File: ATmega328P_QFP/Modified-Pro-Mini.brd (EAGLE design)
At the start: 18.3 x 33.5 mm, 17 parts, among them Q1 8/16/20MHz, U1 ATMEGA328

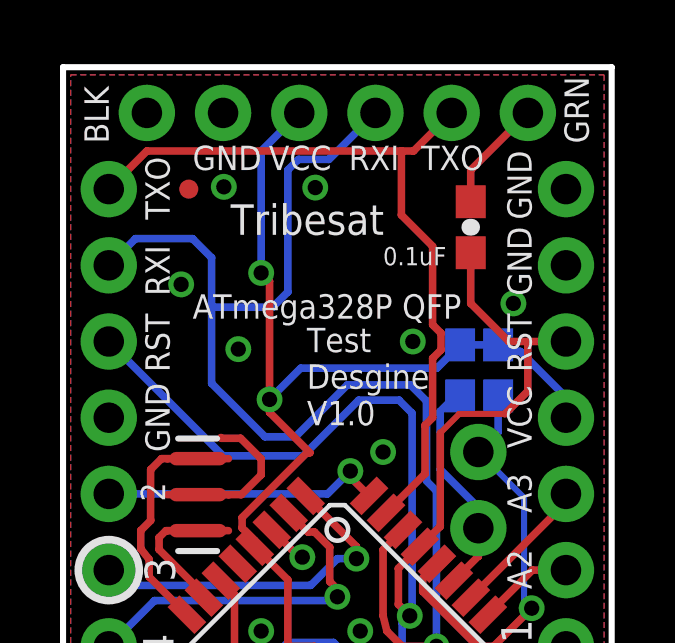
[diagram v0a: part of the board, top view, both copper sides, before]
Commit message: added decoupling cap
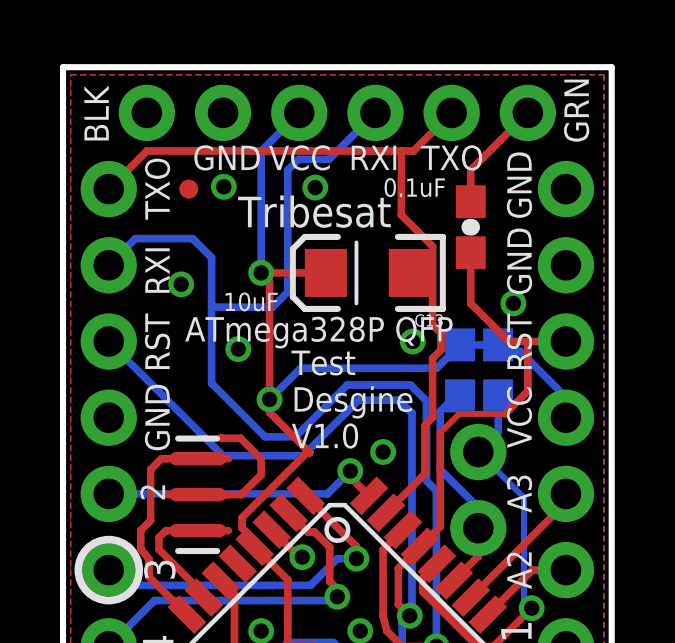
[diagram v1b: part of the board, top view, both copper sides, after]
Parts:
- added C13: 10uF, SparkFun:EIA3216
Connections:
- net GND: now also C13.C
- net VCC: now also C13.A
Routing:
- net VCC: track 54.4 -> 56.6 mm
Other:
- board text added: "10uF"
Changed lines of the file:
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@@
 <rectangle x1="5.334" y1="0.635" x2="5.969" y2="1.27" layer="22"/>
 <text x="15.367" y="28.194" size="0.8128" layer="21" ratio="15" rot="R90">GND</text>
-<text x="5.334" y="27.686" size="1.016" layer="21" font="vector" ratio="15">Tribesat</text>
-<text x="4.064" y="24.892" size="0.8128" layer="21" font="vector" ratio="15">ATmega328P QFP</text>
-<text x="7.874" y="21.336" size="0.8128" layer="21" font="vector" ratio="15">Test
+<text x="5.588" y="27.94" size="1.016" layer="21" font="vector" ratio="15">Tribesat</text>
+<text x="3.81" y="24.13" size="0.8128" layer="21" font="vector" ratio="15">ATmega328P QFP</text>
+<text x="7.366" y="20.574" size="0.8128" layer="21" font="vector" ratio="15">Test
 Desgine
 V1.0</text>
@@
 <text x="5.334" y="1.524" size="0.6096" layer="21" font="vector" ratio="13">0.1uF</text>
 <text x="6.604" y="3.81" size="0.6096" layer="21" font="vector" ratio="13">10k</text>
-<text x="10.414" y="26.67" size="0.6096" layer="21" font="vector" ratio="13">0.1uF</text>
+<text x="10.414" y="28.956" size="0.6096" layer="21" font="vector" ratio="13">0.1uF</text>
 <text x="5.334" y="28.702" size="1.016" layer="22" font="vector" ratio="16" rot="MR180">Tribesat</text>
 <text x="14.224" y="24.892" size="0.8128" layer="22" font="vector" ratio="16" rot="MR0">ATmega328P QFP</text>
@@
 Desgine
 V1.0</text>
+<text x="5.08" y="25.146" size="0.6096" layer="21" font="vector" ratio="13">10uF</text>
 </plain>
 <attributes>
@@
 <attribute name="VALUE" x="14.478" y="26.924" size="0.4064" layer="27" font="vector" rot="R90"/>
 </element>
+<element name="C13" library="SparkFun" package="EIA3216" value="10uF" x="9.906" y="26.416" rot="R180"/>
 </elements>
 <signals>
@@
 <via x="12.7" y="5.588" extent="1-16" drill="0.508"/>
 <contactref element="JP6" pad="1"/>
+<contactref element="C13" pad="C"/>
 </signal>
 <signal name="AREF">
@@
 <wire x1="6.6294" y1="22.1996" x2="6.6294" y2="26.1366" width="0.254" layer="1"/>
 <wire x1="6.6294" y1="26.1366" x2="6.35" y2="26.416" width="0.254" layer="1"/>
+<contactref element="C13" pad="A"/>
+<wire x1="6.35" y1="26.416" x2="8.506" y2="26.416" width="0.254" layer="1"/>
 </signal>
 <signal name="D9">

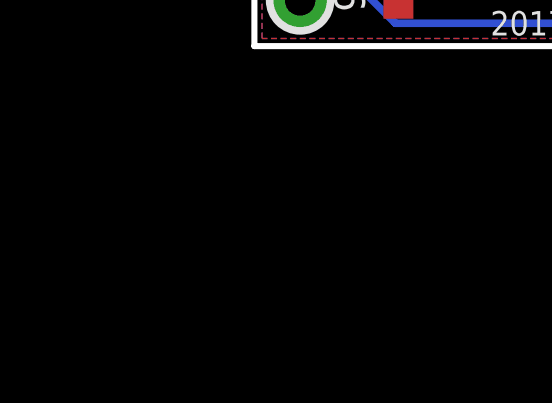
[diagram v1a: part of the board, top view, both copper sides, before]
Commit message: added decoupling cap
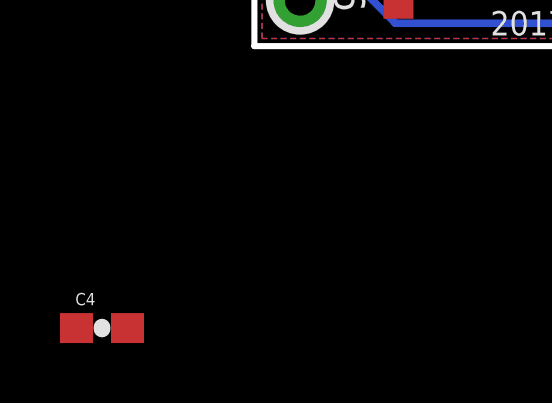
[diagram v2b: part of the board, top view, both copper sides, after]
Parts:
- added C4: 0.1uF, SparkFun:0603-CAP
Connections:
- net GND: now also C4.1
- net VCC: now also C4.2
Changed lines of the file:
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@@
 </element>
 <element name="C13" library="SparkFun" package="EIA3216" value="10uF" x="9.906" y="26.416" rot="R180"/>
+<element name="C4" library="SparkFun" package="0603-CAP" value="0.1uF" x="-5.334" y="-9.652"/>
 </elements>
 <signals>
@@
 <contactref element="JP6" pad="1"/>
 <contactref element="C13" pad="C"/>
+<contactref element="C4" pad="1"/>
+<wire x1="16.51" y1="26.67" x2="16.51" y2="29.21" width="0" layer="19" extent="1-1"/>
+<wire x1="14.7574" y1="25.4" x2="16.51" y2="26.67" width="0" layer="19" extent="1-1"/>
+<wire x1="11.306" y1="26.416" x2="14.7574" y2="25.4" width="0" layer="19" extent="1-1"/>
+<wire x1="11.4046" y1="24.13" x2="11.306" y2="26.416" width="0" layer="19" extent="1-1"/>
+<wire x1="10.414" y1="20.447" x2="11.4046" y2="24.13" width="0" layer="19" extent="1-1"/>
+<wire x1="6.35" y1="20.2184" x2="10.414" y2="20.447" width="0" layer="19" extent="1-1"/>
+<wire x1="6.7032" y1="17.853853125" x2="5.6896" y2="19.0246" width="0" layer="19" extent="1-1"/>
+<wire x1="7.7216" y1="16.9418" x2="7.666053125" y2="16.891" width="0" layer="19" extent="1-1"/>
+<wire x1="5.571828125" y1="16.72248125" x2="6.7032" y2="17.853853125" width="0" layer="19" extent="1-1"/>
+<wire x1="6.35" y1="14.478" x2="5.571828125" y2="16.72248125" width="0" layer="19" extent="1-1"/>
+<wire x1="5.588" y1="23.876" x2="5.6642" y2="20.9042" width="0" layer="19" extent="1-1"/>
+<wire x1="3.683" y1="26.035" x2="5.588" y2="23.876" width="0" layer="19" extent="1-1"/>
+<wire x1="9.652" y1="14.478" x2="7.747" y2="16.891" width="0" layer="19" extent="1-1"/>
+<wire x1="11.43" y1="12.7" x2="9.652" y2="14.478" width="0" layer="19" extent="1-1"/>
+<wire x1="12.20816875" y1="11.217515625" x2="11.43" y2="12.7" width="0" layer="19" extent="1-1"/>
+<wire x1="1.27" y1="21.59" x2="3.2258" y2="19.0246" width="0" layer="19" extent="1-1"/>
+<wire x1="5.1054" y1="29.2862" x2="3.683" y2="26.035" width="0" layer="19" extent="1-1"/>
+<wire x1="5.08" y1="31.75" x2="5.1054" y2="29.2862" width="0" layer="19" extent="1-1"/>
+<wire x1="2.54" y1="31.75" x2="5.08" y2="31.75" width="0" layer="19" extent="1-1"/>
+<wire x1="8.1534" y1="29.2608" x2="5.1054" y2="29.2862" width="0" layer="19" extent="1-1"/>
+<wire x1="9.867" y1="7.239" x2="12.20816875" y2="11.217515625" width="0" layer="19" extent="1-1"/>
+<wire x1="12.7" y1="5.588" x2="9.867" y2="7.239" width="0" layer="19" extent="1-1"/>
+<wire x1="12.0262" y1="1.524" x2="12.7" y2="5.588" width="0" layer="19" extent="1-1"/>
+<wire x1="8.89" y1="2.667" x2="12.0262" y2="1.524" width="0" layer="19" extent="1-1"/>
+<wire x1="5.969" y1="1.651" x2="8.89" y2="2.667" width="0" layer="19" extent="1-1"/>
+<wire x1="-6.184" y1="-9.652" x2="4.5466" y2="1.2074" width="0" layer="19" extent="1-1"/>
 </signal>
 <signal name="AREF">
@@
 <contactref element="C13" pad="A"/>
 <wire x1="6.35" y1="26.416" x2="8.506" y2="26.416" width="0.254" layer="1"/>
+<contactref element="C4" pad="2"/>
+<wire x1="4.865" y1="5.08" x2="-4.484" y2="-9.652" width="0" layer="19" extent="1-1"/>
 </signal>
 <signal name="D9">

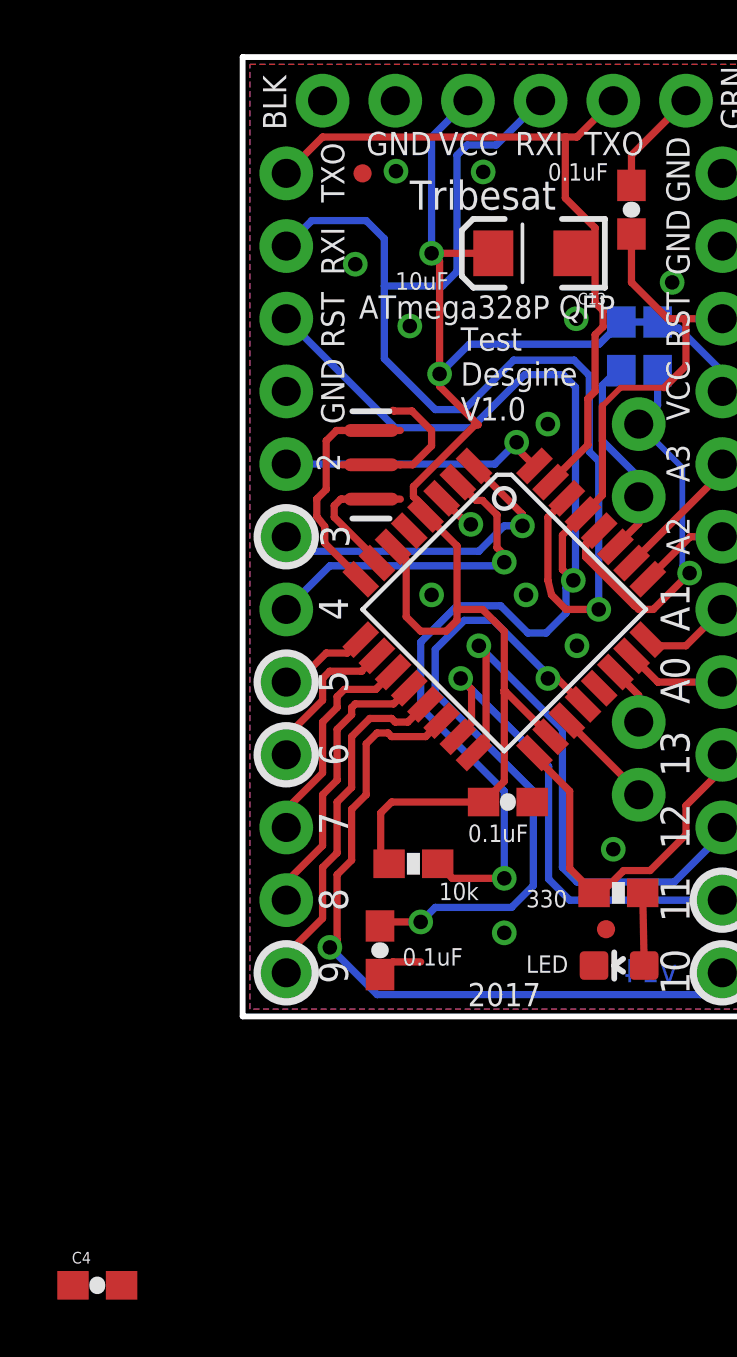
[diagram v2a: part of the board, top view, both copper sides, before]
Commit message: palced decoupling cap
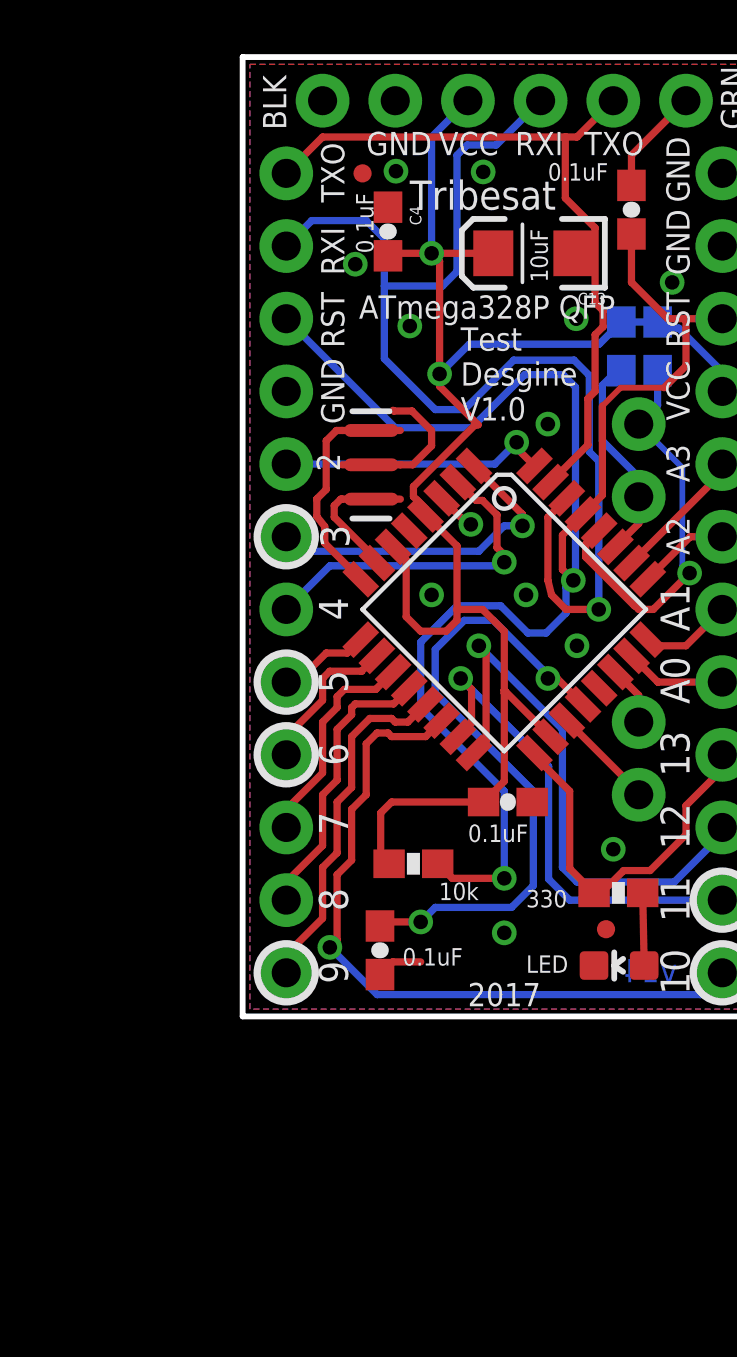
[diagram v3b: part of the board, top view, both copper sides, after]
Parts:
- moved C4 38.2 mm to (4.83, 27.2), turned to 270 degrees
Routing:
- net VCC: track 56.6 -> 58.2 mm
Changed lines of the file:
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@@
 Desgine
 V1.0</text>
-<text x="5.08" y="25.146" size="0.6096" layer="21" font="vector" ratio="13">10uF</text>
+<text x="10.414" y="25.4" size="0.6096" layer="21" font="vector" ratio="13" rot="R90">10uF</text>
+<text x="4.318" y="26.416" size="0.6096" layer="21" font="vector" ratio="13" rot="R90">0.1uF</text>
 </plain>
 <attributes>
@@
 </element>
 <element name="C13" library="SparkFun" package="EIA3216" value="10uF" x="9.906" y="26.416" rot="R180"/>
-<element name="C4" library="SparkFun" package="0603-CAP" value="0.1uF" x="-5.334" y="-9.652"/>
+<element name="C4" library="SparkFun" package="0603-CAP" value="0.1uF" x="4.826" y="27.178" rot="R270"/>
 </elements>
 <signals>
@@
 <contactref element="C13" pad="C"/>
 <contactref element="C4" pad="1"/>
-<wire x1="16.51" y1="26.67" x2="16.51" y2="29.21" width="0" layer="19" extent="1-1"/>
-<wire x1="14.7574" y1="25.4" x2="16.51" y2="26.67" width="0" layer="19" extent="1-1"/>
-<wire x1="11.306" y1="26.416" x2="14.7574" y2="25.4" width="0" layer="19" extent="1-1"/>
-<wire x1="11.4046" y1="24.13" x2="11.306" y2="26.416" width="0" layer="19" extent="1-1"/>
-<wire x1="10.414" y1="20.447" x2="11.4046" y2="24.13" width="0" layer="19" extent="1-1"/>
-<wire x1="6.35" y1="20.2184" x2="10.414" y2="20.447" width="0" layer="19" extent="1-1"/>
-<wire x1="6.7032" y1="17.853853125" x2="5.6896" y2="19.0246" width="0" layer="19" extent="1-1"/>
-<wire x1="7.7216" y1="16.9418" x2="7.666053125" y2="16.891" width="0" layer="19" extent="1-1"/>
-<wire x1="5.571828125" y1="16.72248125" x2="6.7032" y2="17.853853125" width="0" layer="19" extent="1-1"/>
-<wire x1="6.35" y1="14.478" x2="5.571828125" y2="16.72248125" width="0" layer="19" extent="1-1"/>
-<wire x1="5.588" y1="23.876" x2="5.6642" y2="20.9042" width="0" layer="19" extent="1-1"/>
-<wire x1="3.683" y1="26.035" x2="5.588" y2="23.876" width="0" layer="19" extent="1-1"/>
-<wire x1="9.652" y1="14.478" x2="7.747" y2="16.891" width="0" layer="19" extent="1-1"/>
-<wire x1="11.43" y1="12.7" x2="9.652" y2="14.478" width="0" layer="19" extent="1-1"/>
-<wire x1="12.20816875" y1="11.217515625" x2="11.43" y2="12.7" width="0" layer="19" extent="1-1"/>
-<wire x1="1.27" y1="21.59" x2="3.2258" y2="19.0246" width="0" layer="19" extent="1-1"/>
-<wire x1="5.1054" y1="29.2862" x2="3.683" y2="26.035" width="0" layer="19" extent="1-1"/>
-<wire x1="5.08" y1="31.75" x2="5.1054" y2="29.2862" width="0" layer="19" extent="1-1"/>
-<wire x1="2.54" y1="31.75" x2="5.08" y2="31.75" width="0" layer="19" extent="1-1"/>
-<wire x1="8.1534" y1="29.2608" x2="5.1054" y2="29.2862" width="0" layer="19" extent="1-1"/>
-<wire x1="9.867" y1="7.239" x2="12.20816875" y2="11.217515625" width="0" layer="19" extent="1-1"/>
-<wire x1="12.7" y1="5.588" x2="9.867" y2="7.239" width="0" layer="19" extent="1-1"/>
-<wire x1="12.0262" y1="1.524" x2="12.7" y2="5.588" width="0" layer="19" extent="1-1"/>
-<wire x1="8.89" y1="2.667" x2="12.0262" y2="1.524" width="0" layer="19" extent="1-1"/>
-<wire x1="5.969" y1="1.651" x2="8.89" y2="2.667" width="0" layer="19" extent="1-1"/>
-<wire x1="-6.184" y1="-9.652" x2="4.5466" y2="1.2074" width="0" layer="19" extent="1-1"/>
 </signal>
 <signal name="AREF">
@@
 <wire x1="6.35" y1="26.416" x2="8.506" y2="26.416" width="0.254" layer="1"/>
 <contactref element="C4" pad="2"/>
-<wire x1="4.865" y1="5.08" x2="-4.484" y2="-9.652" width="0" layer="19" extent="1-1"/>
+<wire x1="6.35" y1="26.416" x2="4.914" y2="26.416" width="0.254" layer="1"/>
+<wire x1="4.914" y1="26.416" x2="4.826" y2="26.328" width="0.254" layer="1"/>
 </signal>
 <signal name="D9">

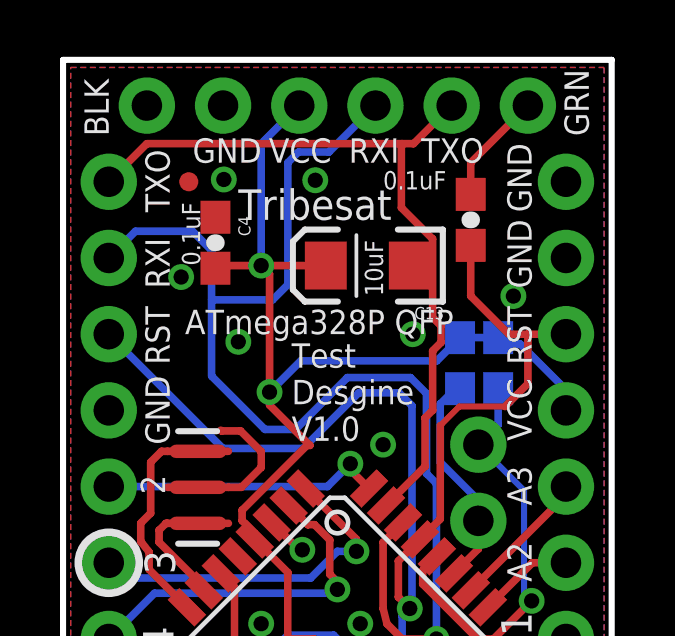
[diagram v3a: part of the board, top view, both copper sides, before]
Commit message: fixed DRC errors
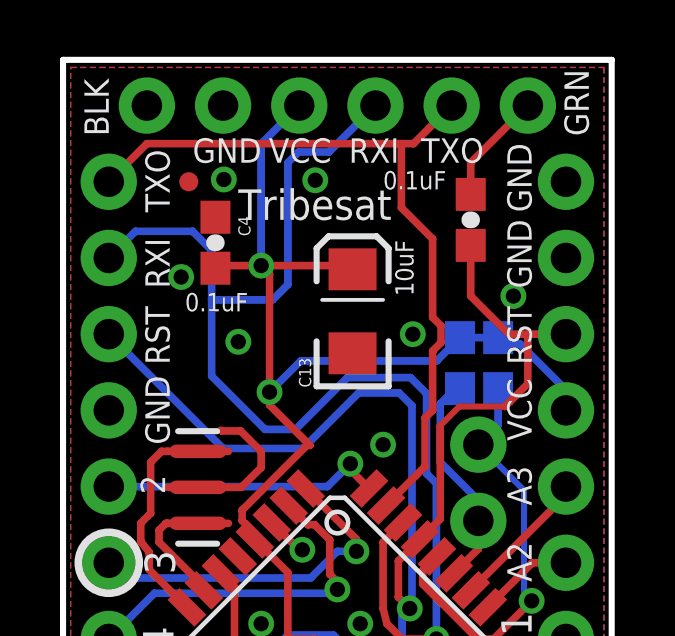
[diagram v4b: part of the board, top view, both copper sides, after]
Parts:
- moved C13 1.61 mm to (9.40, 24.9), turned to 90 degrees
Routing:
- net VCC: track 58.2 -> 59.1 mm
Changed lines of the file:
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@@
 <text x="15.367" y="28.194" size="0.8128" layer="21" ratio="15" rot="R90">GND</text>
 <text x="5.588" y="27.94" size="1.016" layer="21" font="vector" ratio="15">Tribesat</text>
-<text x="3.81" y="24.13" size="0.8128" layer="21" font="vector" ratio="15">ATmega328P QFP</text>
-<text x="7.366" y="20.574" size="0.8128" layer="21" font="vector" ratio="15">Test
-Desgine
-V1.0</text>
 <text x="8.89" y="0.508" size="0.8128" layer="21" font="vector" ratio="15" align="center">2017</text>
 <text x="7.62" y="5.842" size="0.6096" layer="21" font="vector" ratio="13">0.1uF</text>
@@
 Desgine
 V1.0</text>
-<text x="10.414" y="25.4" size="0.6096" layer="21" font="vector" ratio="13" rot="R90">10uF</text>
-<text x="4.318" y="26.416" size="0.6096" layer="21" font="vector" ratio="13" rot="R90">0.1uF</text>
+<text x="11.43" y="25.4" size="0.6096" layer="21" font="vector" ratio="13" rot="R90">10uF</text>
+<text x="3.81" y="24.892" size="0.6096" layer="21" font="vector" ratio="13">0.1uF</text>
 </plain>
 <attributes>
@@
 <attribute name="VALUE" x="14.478" y="26.924" size="0.4064" layer="27" font="vector" rot="R90"/>
 </element>
-<element name="C13" library="SparkFun" package="EIA3216" value="10uF" x="9.906" y="26.416" rot="R180"/>
+<element name="C13" library="SparkFun" package="EIA3216" value="10uF" x="9.398" y="24.892" rot="R90"/>
 <element name="C4" library="SparkFun" package="0603-CAP" value="0.1uF" x="4.826" y="27.178" rot="R270"/>
 </elements>
@@
 <wire x1="6.6294" y1="26.1366" x2="6.35" y2="26.416" width="0.254" layer="1"/>
 <contactref element="C13" pad="A"/>
-<wire x1="6.35" y1="26.416" x2="8.506" y2="26.416" width="0.254" layer="1"/>
 <contactref element="C4" pad="2"/>
 <wire x1="6.35" y1="26.416" x2="4.914" y2="26.416" width="0.254" layer="1"/>
 <wire x1="4.914" y1="26.416" x2="4.826" y2="26.328" width="0.254" layer="1"/>
+<wire x1="6.35" y1="26.416" x2="9.274" y2="26.416" width="0.254" layer="1"/>
+<wire x1="9.274" y1="26.416" x2="9.398" y2="26.292" width="0.254" layer="1"/>
 </signal>
 <signal name="D9">
